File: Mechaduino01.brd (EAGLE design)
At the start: 41.9 x 41.9 mm, 68 parts, among them IC1 SAMD21G18A-AUT, IC2 AP2112K-3.3, Q1 2.5A/30V, Q2 NFET, Q3 BSS138, Q4 BSS138, U3 74AHC1G125, Y1 32,768Khz

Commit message: 100k to 100K
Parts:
- R16: value 100k -> 100K
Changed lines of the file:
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@@
 <element name="U$3" library="stepper_servo_prototype_1" package="LOGO3" value="TROPICAL_LABS_LOGO_1LOGO3" x="6.096" y="12.192" rot="R90"/>
 <element name="J1" library="MF_Connectors" package="MICROUSB-RIGHT" value="" x="38.735" y="20.166" locked="yes" smashed="yes" rot="R90"/>
-<element name="R16" library="adafruit" package="R0402-VISHAY" value="100k" x="3.175" y="27.813" rot="MR180"/>
+<element name="R16" library="adafruit" package="R0402-VISHAY" value="100K" x="3.175" y="27.813" rot="MR180"/>
 <element name="F1" library="SparkFun-PowerIC" package="PTC-1206" value="500mA" x="20.574" y="15.621" smashed="yes" rot="MR0">
 <attribute name="PROD_ID" value="RES-11150" x="30.099" y="23.876" size="1.778" layer="28" rot="MR0" display="off"/>

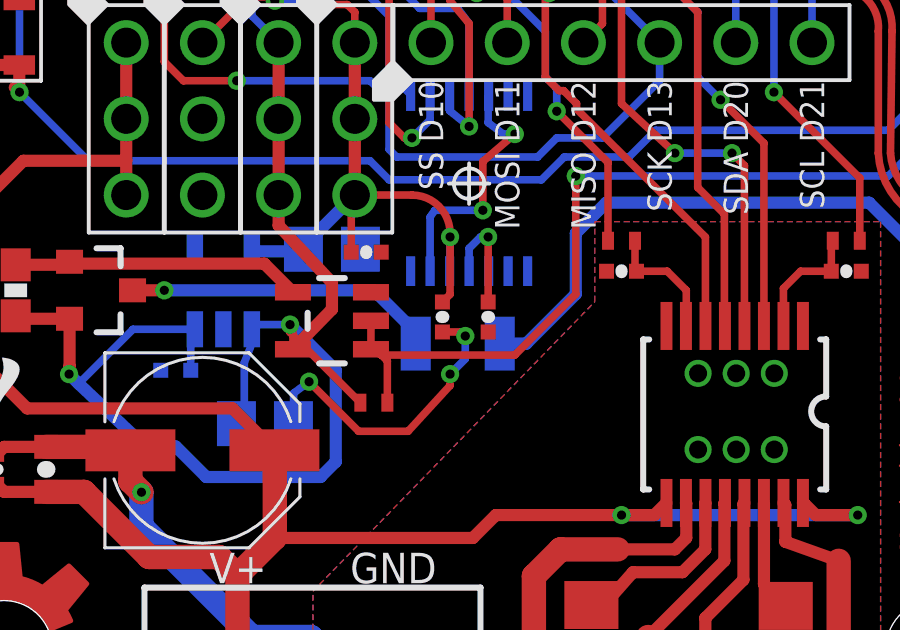
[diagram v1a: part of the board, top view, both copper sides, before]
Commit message: minor change to as5047 power circuit
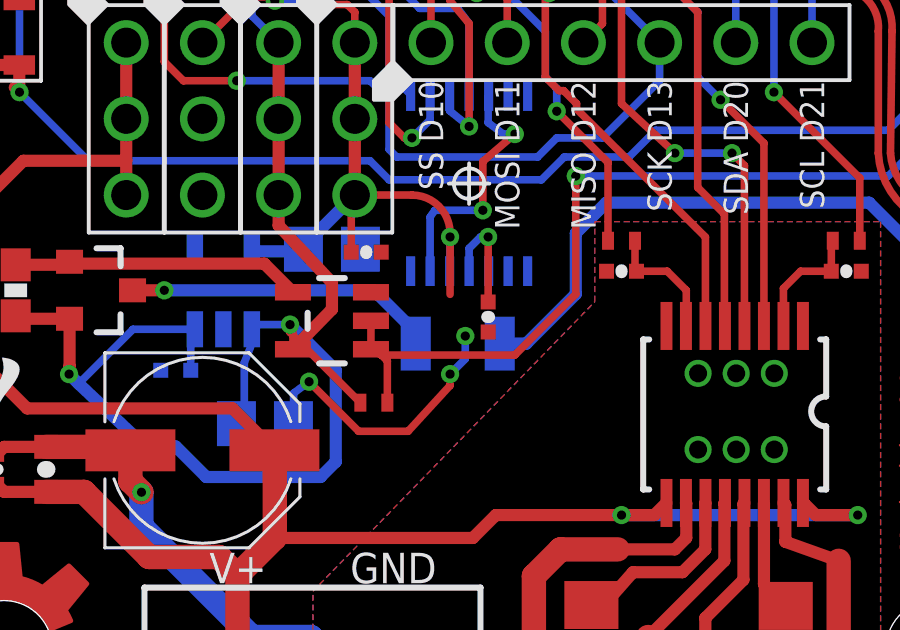
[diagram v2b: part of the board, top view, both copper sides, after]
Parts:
- removed C17: 1uF, swift:0402-CAP
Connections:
- removed net N$27: C16.1, U$4.11
- net 3.3V: now also C16.1, U$4.11; no longer C17.1
- net GND: no longer C17.2
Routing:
- net N$27: track 3.72 -> 0.00 mm, vias 1 -> 0
- net 3.3V: track 88.4 -> 91.8 mm, vias 3 -> 4
- net GND: track 76.7 -> 76.0 mm
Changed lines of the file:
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@@
 <?xml version="1.0" encoding="utf-8"?>
 <!DOCTYPE eagle SYSTEM "eagle.dtd">
-<eagle version="7.3.0">
+<eagle version="7.7.0">
 <drawing>
 <settings>
@@
 </element>
 <element name="C16" library="swift" package="0402-CAP" value="0.1uF" x="21.59" y="16.51" smashed="yes" rot="R270"/>
-<element name="C17" library="swift" package="0402-CAP" value="1uF" x="20.066" y="16.51" smashed="yes" rot="R270">
-<attribute name="VALUE" x="18.923" y="17.5895" size="0.4064" layer="27" rot="R270"/>
-</element>
 <element name="SH1" library="shorts-old" package="SHORT_ALL-50" value="SHORT-HA5" x="15.875" y="1.27" smashed="yes" rot="R180">
 <attribute name="BOM" value="no" x="15.875" y="1.27" size="1.778" layer="27" rot="R180" display="off"/>
@@
 <contactref element="U$4" pad="5"/>
 <contactref element="C16" pad="2"/>
-<contactref element="C17" pad="2"/>
 <polygon width="0.2032" layer="16" isolate="0.254" rank="2">
 <vertex x="-0.635" y="-0.635"/>
@@
 <via x="20.828" y="15.875" extent="1-16" drill="0.3048"/>
 <wire x1="20.828" y1="15.875" x2="20.693" y2="16.01" width="0.254" layer="1"/>
-<wire x1="20.693" y1="16.01" x2="20.066" y2="16.01" width="0.254" layer="1"/>
 <wire x1="26.297" y1="37.084" x2="27.043" y2="37.83" width="0.254" layer="1"/>
 <wire x1="27.043" y1="37.83" x2="27.043" y2="38.227" width="0.254" layer="1"/>
 <contactref element="SW2" pad="P$3"/>
 <contactref element="SW2" pad="P$4"/>
+<wire x1="39.497" y1="30.226" x2="39.497" y2="28.956" width="0" layer="19" extent="1-1"/>
+<wire x1="39.497" y1="26.416" x2="39.497" y2="28.956" width="0" layer="19" extent="1-1"/>
+<wire x1="36.957" y1="30.353" x2="39.497" y2="30.226" width="0" layer="19" extent="1-1"/>
+<wire x1="24.765" y1="34.417" x2="26.96586875" y2="31.84210625" width="0" layer="19" extent="1-16"/>
+<wire x1="18.407" y1="38.862" x2="18.407" y2="37.592" width="0" layer="19" extent="16-16"/>
+<wire x1="12.065" y1="23.114" x2="12.065" y2="25.654" width="0" layer="19" extent="1-1"/>
+<wire x1="12.065" y1="20.574" x2="12.065" y2="23.114" width="0" layer="19" extent="1-1"/>
+<wire x1="12.7635" y1="16.0989" x2="12.065" y2="20.574" width="0" layer="19" extent="16-16"/>
+<wire x1="10.676" y1="14.732" x2="12.7635" y2="16.0989" width="0" layer="19" extent="16-16"/>
+<wire x1="15.105" y1="13.97" x2="12.7635" y2="16.0989" width="0" layer="19" extent="16-16"/>
+<wire x1="21.59" y1="16.01" x2="20.828" y2="15.875" width="0" layer="19" extent="1-1"/>
+<wire x1="19.655" y1="18.0372" x2="20.693" y2="16.01" width="0" layer="19" extent="1-16"/>
+<wire x1="18.026" y1="18.669" x2="19.655" y2="18.0372" width="0" layer="19" extent="1-16"/>
+<wire x1="17.333" y1="18.769" x2="18.026" y2="18.669" width="0" layer="19" extent="1-16"/>
+<wire x1="17.6831" y1="17.333" x2="18.026" y2="18.669" width="0" layer="19" extent="1-1"/>
+<wire x1="37.465" y1="21.466" x2="39.497" y2="26.416" width="0" layer="19" extent="1-1"/>
+<wire x1="5.9612" y1="27.0592" x2="12.065" y2="25.654" width="0" layer="19" extent="1-1"/>
+<wire x1="2.725" y1="27.813" x2="5.9612" y2="27.0592" width="0" layer="19" extent="1-16"/>
+<wire x1="2.525" y1="28.92" x2="2.725" y2="27.813" width="0" layer="19" extent="16-16"/>
+<wire x1="1.8112" y1="27.0592" x2="2.725" y2="27.813" width="0" layer="19" extent="1-16"/>
+<wire x1="15.24" y1="1.27" x2="17.272" y2="12.7" width="0" layer="19" extent="1-1"/>
 </signal>
 <signal name="RESET">
@@
 <contactref element="C10" pad="1"/>
 <contactref element="U$4" pad="12"/>
-<contactref element="C17" pad="1"/>
 <contactref element="Q4" pad="1"/>
 <contactref element="Q3" pad="1"/>
@@
 <wire x1="20.32" y1="19.177" x2="20.32" y2="18.0522" width="0.254" layer="16"/>
 <wire x1="20.32" y1="18.0522" x2="20.305" y2="18.0372" width="0.254" layer="16" curve="-90"/>
-<wire x1="20.066" y1="17.01" x2="20.32" y2="17.264" width="0.254" layer="1"/>
 <wire x1="20.32" y1="17.264" x2="20.32" y2="19.177" width="0.254" layer="1"/>
 <wire x1="17.145" y1="25.654" x2="17.145" y2="23.114" width="0.4064" layer="1"/>
@@
 <wire x1="15.621" y1="26.924" x2="14.913890625" y2="27.631109375" width="0.254" layer="1"/>
 <wire x1="14.913890625" y1="27.631109375" x2="14.913890625" y2="28.194" width="0.254" layer="1"/>
+<contactref element="U$4" pad="11"/>
+<contactref element="C16" pad="1"/>
+<wire x1="21.59" y1="17.01" x2="21.59" y2="19.177" width="0.254" layer="1"/>
+<via x="21.59" y="19.177" extent="1-16" drill="0.3048"/>
+<wire x1="21.59" y1="19.177" x2="21.336" y2="19.177" width="0.254" layer="16"/>
+<wire x1="21.336" y1="19.177" x2="20.955" y2="18.796" width="0.254" layer="16"/>
+<wire x1="20.955" y1="18.796" x2="20.955" y2="18.0372" width="0.254" layer="16"/>
+<wire x1="20.32" y1="18.0522" x2="20.955" y2="18.0372" width="0" layer="19" extent="16-16"/>
 </signal>
 <signal name="ARDUINO_D12_MISO">
@@
 <wire x1="29.464" y1="10.2917" x2="29.4827" y2="10.3104" width="0.4064" layer="1"/>
 </signal>
-<signal name="N$27">
-<contactref element="U$4" pad="11"/>
-<contactref element="C16" pad="1"/>
-<wire x1="21.59" y1="17.01" x2="21.59" y2="19.177" width="0.254" layer="1"/>
-<via x="21.59" y="19.177" extent="1-16" drill="0.3048"/>
-<wire x1="21.59" y1="19.177" x2="21.336" y2="19.177" width="0.254" layer="16"/>
-<wire x1="21.336" y1="19.177" x2="20.955" y2="18.796" width="0.254" layer="16"/>
-<wire x1="20.955" y1="18.796" x2="20.955" y2="18.0372" width="0.254" layer="16"/>
-</signal>
 <signal name="N$32">

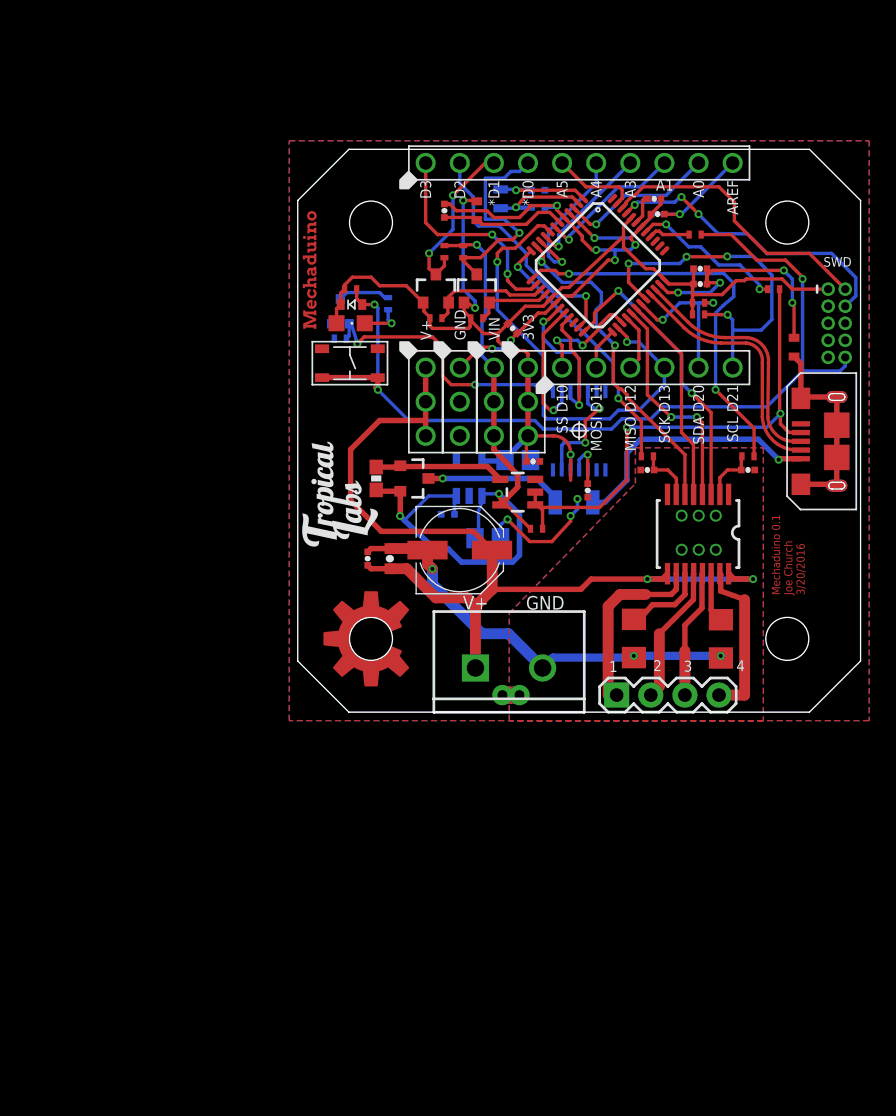
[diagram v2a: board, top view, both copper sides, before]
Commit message: added third level shifter (same as others)
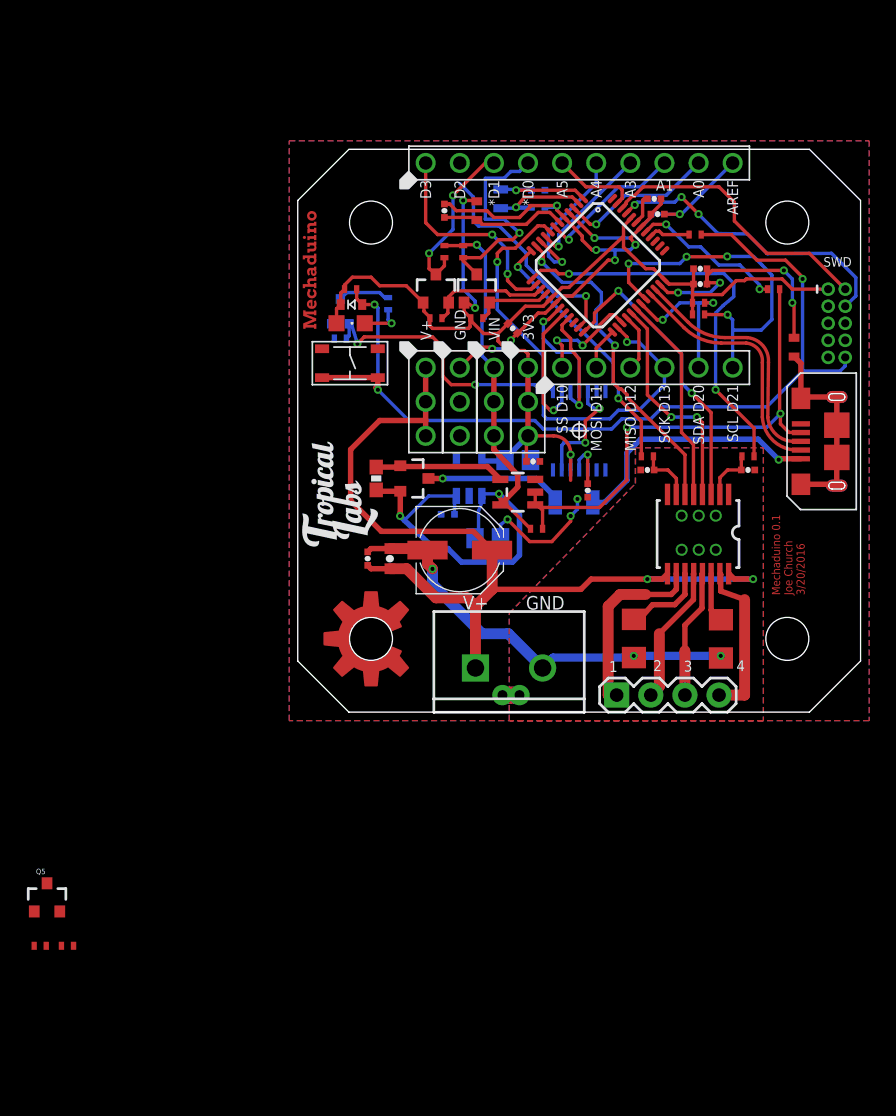
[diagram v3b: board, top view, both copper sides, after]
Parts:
- added Q5: BSS138, SparkFun:SOT23-3
- added R11, R4: 10K, adafruit:R0402-VISHAY
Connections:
- new net HV3: J2.P$2, Q5.3, R11.1
- net 3.3V: now also Q5.1, R4.2
- net ARDUINO_D2: now also Q5.2, R4.1; no longer J2.P$2
- net VIN: now also R11.2
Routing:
- net ARDUINO_D2: track 18.6 -> 17.0 mm
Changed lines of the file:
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@@
 <element name="U$5" library="stepper_servo_prototype_1" package="MECHADUINO_LOGO" value="MECHADUINO_LOGO" x="1.524" y="28.448" rot="R90"/>
 <element name="SW2" library="MF_Switches" package="TACT4.2MM" value="" x="3.8862" y="25.9842" smashed="yes" rot="R180"/>
+<element name="Q5" library="SparkFun" package="SOT23-3" value="BSS138" x="-18.669" y="-13.843"/>
+<element name="R4" library="adafruit" package="R0402-VISHAY" value="10K" x="-19.177" y="-17.399"/>
+<element name="R11" library="adafruit" package="R0402-VISHAY" value="10K" x="-17.145" y="-17.399"/>
 </elements>
 <signals>
@@
 <wire x1="21.336" y1="19.177" x2="20.955" y2="18.796" width="0.254" layer="16"/>
 <wire x1="20.955" y1="18.796" x2="20.955" y2="18.0372" width="0.254" layer="16"/>
+<contactref element="Q5" pad="1"/>
+<contactref element="R4" pad="2"/>
 <wire x1="20.32" y1="18.0522" x2="20.955" y2="18.0372" width="0" layer="19" extent="16-16"/>
+<wire x1="-19.619" y1="-14.843" x2="13.7135" y2="18.6991" width="0" layer="19" extent="1-16"/>
+<wire x1="-18.727" y1="-17.399" x2="-19.619" y2="-14.843" width="0" layer="19" extent="1-1"/>
 </signal>
 <signal name="ARDUINO_D12_MISO">
@@
 <signal name="ARDUINO_D2">
 <contactref element="IC1" pad="23"/>
-<contactref element="J2" pad="P$2"/>
-<wire x1="12.065" y1="40.894" x2="12.065" y2="39.37" width="0.254" layer="16"/>
 <wire x1="12.065" y1="39.37" x2="13.081" y2="38.354" width="0.254" layer="16"/>
 <wire x1="13.081" y1="38.354" x2="13.081" y2="36.576" width="0.254" layer="16"/>
@@
 <wire x1="21.463" y1="30.988" x2="21.463" y2="29.203021875" width="0.254" layer="1"/>
 <wire x1="21.463" y1="29.203021875" x2="20.92010625" y2="28.660128125" width="0.254" layer="1"/>
+<contactref element="R4" pad="1"/>
+<contactref element="Q5" pad="2"/>
+<wire x1="-17.719" y1="-14.843" x2="20.92010625" y2="28.660128125" width="0" layer="19" extent="1-1"/>
+<wire x1="-19.627" y1="-17.399" x2="-17.719" y2="-14.843" width="0" layer="19" extent="1-1"/>
 </signal>
 <signal name="ARDUINO_D5----IN3">
@@
 <wire x1="11.8135" y1="16.0989" x2="9.7489" y2="16.0989" width="0.254" layer="16"/>
 <wire x1="9.7489" y1="16.0989" x2="7.9375" y2="14.2875" width="0.254" layer="16"/>
+<contactref element="R11" pad="2"/>
+<wire x1="10.16" y1="12.192" x2="-16.695" y2="-17.399" width="0" layer="19" extent="1-16"/>
 </signal>
 <signal name="N$2">
@@
 <wire x1="16.51" y1="40.259" x2="17.145" y2="40.894" width="0.254" layer="16"/>
 </signal>
+<signal name="HV3">
+<contactref element="Q5" pad="3"/>
+<contactref element="R11" pad="1"/>
+<contactref element="J2" pad="P$2"/>
+<wire x1="-18.669" y1="-12.743" x2="12.065" y2="40.894" width="0" layer="19" extent="1-1"/>
+<wire x1="-17.595" y1="-17.399" x2="-18.669" y2="-12.743" width="0" layer="19" extent="1-1"/>
+</signal>
 </signals>

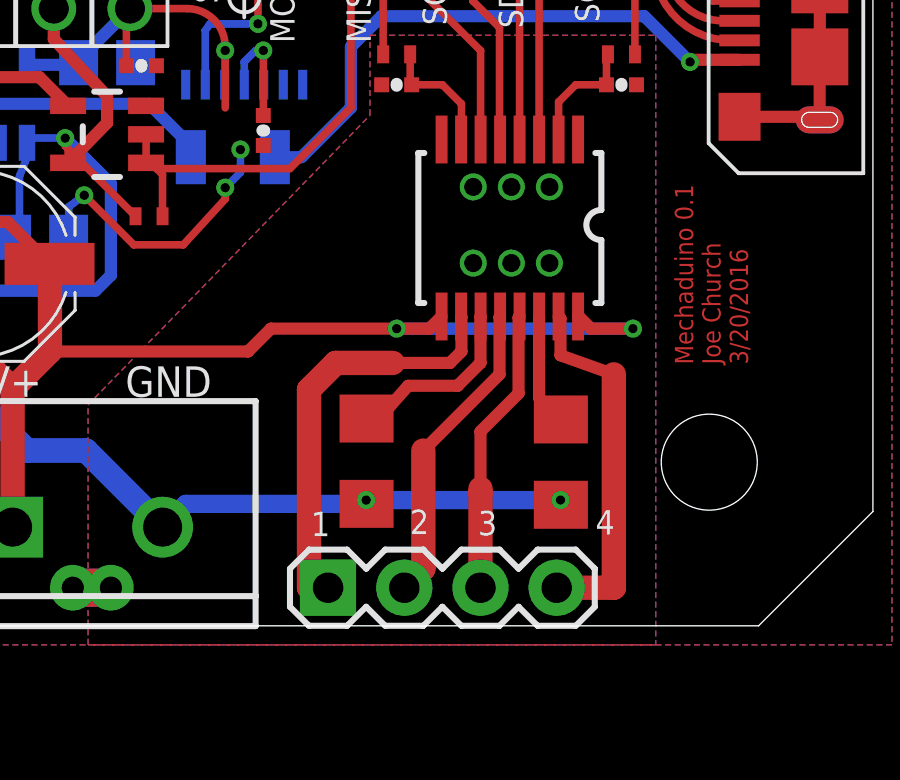
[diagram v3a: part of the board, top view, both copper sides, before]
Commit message: fixed thermal and a4954 clearance
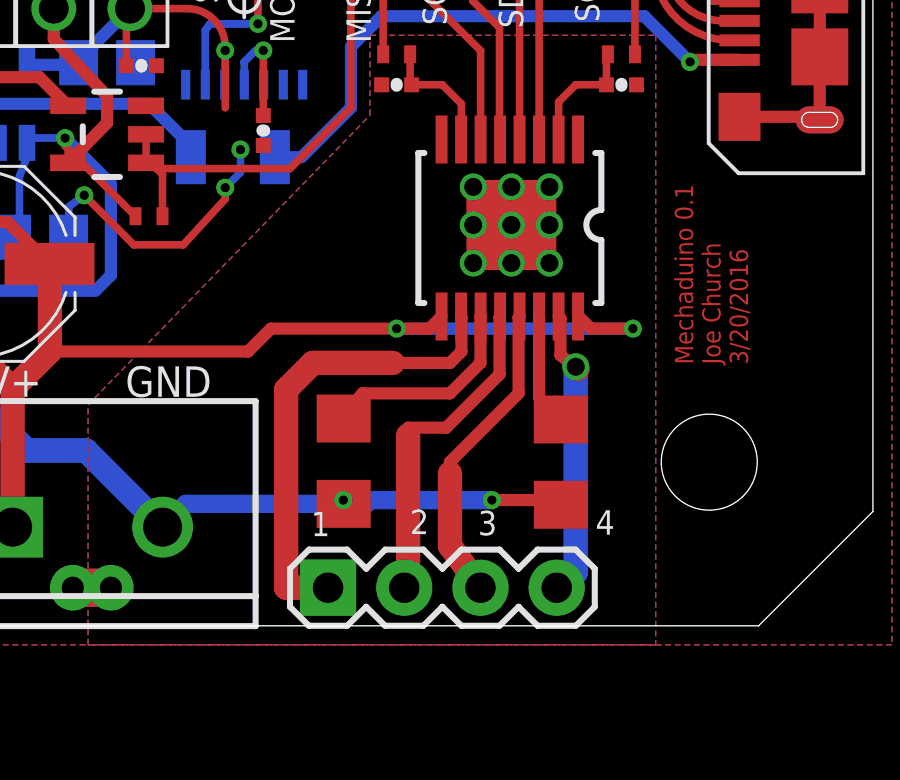
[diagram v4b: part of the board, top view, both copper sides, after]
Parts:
- IC2: value AP2112K-3.3 -> AP2202-ADJ; device SparkFun-PowerIC:SOT23-5@1 -> SparkFun-PowerIC:SOT23-5$1
- U$1: value AVAGO_DRIVER -> AVAGO_DRIVERTHERM; device avagopack:TSSOP16 -> avagopack:TSSOP16_THERM
- U$2: value NEMA17_HOLE_PATTERN -> NEMA17_HOLE_PATTERNNEW; device stepper_servo_prototype_1:NEMA17_HOLE_PATTERN -> stepper_servo_prototype_1:NEMA17_HOLE_PATTERN_2
- moved R13 0.76 mm to (24.3, 5.49)
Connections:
- net GND2: now also U$1.P$1
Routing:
- net N$16: track 9.71 -> 12.7 mm
- net N$13: track 12.2 -> 9.85 mm, vias 0 -> 1
- net N$14: track 14.0 -> 15.5 mm
- net GND2: track 32.1 -> 33.4 mm, vias 9 -> 12
- net N$4: track 6.15 -> 7.10 mm
- net N$15: track 10.4 -> 11.1 mm
